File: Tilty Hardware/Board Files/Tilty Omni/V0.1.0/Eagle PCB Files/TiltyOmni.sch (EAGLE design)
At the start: 38 parts, among them U1 TEENSY_3.0_ALLPINSTEENSY_3.0_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, U2 HC-09_BREAKOUT, U4 LM2931, U5 MPU-6050, U7 SPI_FLASH-X25XXSMD

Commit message: Tilty omni work
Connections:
- net 5V_SCL: no longer JP7.11
- net 5V_SDA: now also JP7.11
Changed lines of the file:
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@@
 <label x="241.3" y="12.7" size="1.778" layer="95"/>
+</segment>
+<segment>
+<pinref part="JP7" gate="G$1" pin="11"/>
+<wire x1="302.26" y1="78.74" x2="312.42" y2="78.74" width="0.1524" layer="91"/>
+<label x="304.8" y="78.74" size="1.778" layer="95"/>
 </segment>
 </net>
@@
 </segment>
 <segment>
-<pinref part="JP7" gate="G$1" pin="11"/>
-<wire x1="302.26" y1="78.74" x2="312.42" y2="78.74" width="0.1524" layer="91"/>
-<label x="304.8" y="78.74" size="1.778" layer="95"/>
-</segment>
-<segment>

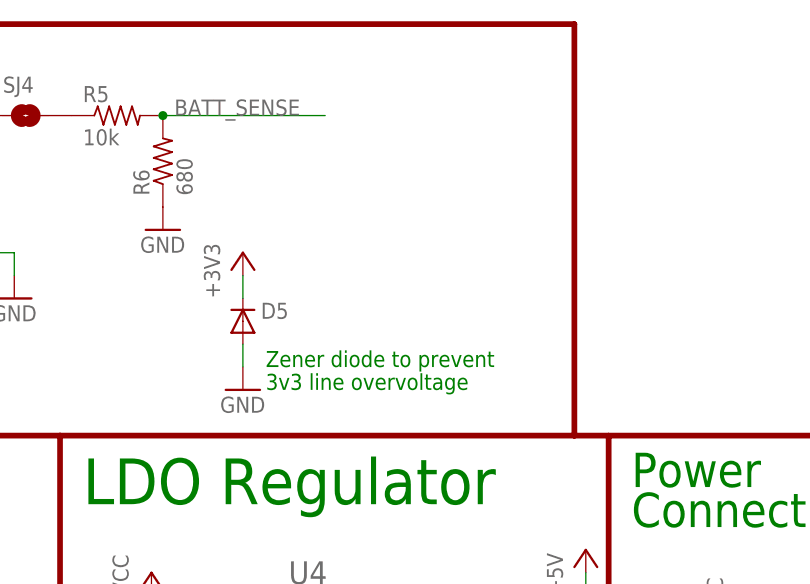
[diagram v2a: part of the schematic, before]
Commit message: Updated Tilty Duo/Quad Things.todo and moved a couple parts on Tilty Omni
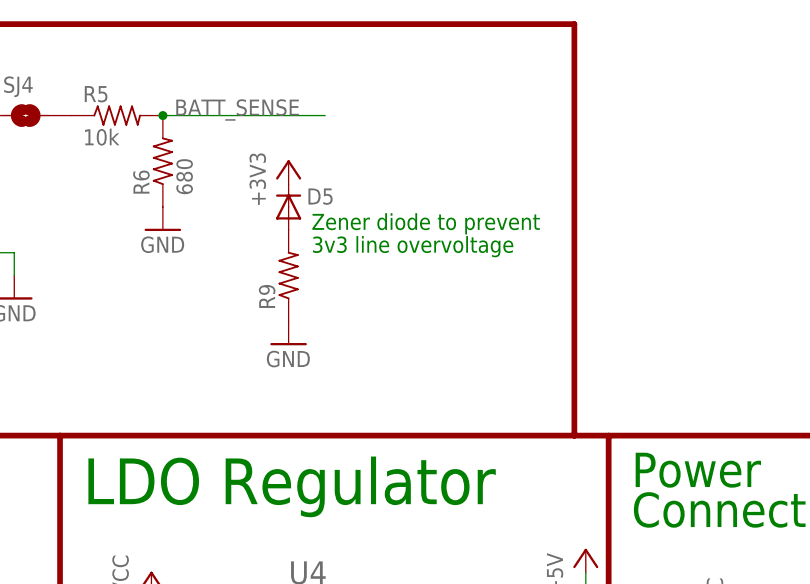
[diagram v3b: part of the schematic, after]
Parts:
- added R9: (no value), resistor:R-US_R0603
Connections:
- new net N$5: D5.A, R9.2
- net GND: now also R9.1; no longer D5.A
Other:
- moved on the sheet: D5
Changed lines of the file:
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@@
 <part name="P+9" library="supply1" deviceset="VCC" device=""/>
 <part name="GND5" library="supply1" deviceset="GND" device=""/>
+<part name="R9" library="resistor" deviceset="R-US_" device="R0603"/>
 </parts>
 <sheets>
@@
 <wire x1="212.725" y1="76.2" x2="172.72" y2="76.2" width="0.635" layer="94"/>
 <text x="7.62" y="172.72" size="5.08" layer="91" ratio="14">Flash Memory</text>
-<text x="134.62" y="142.24" size="1.778" layer="91">Zener diode to prevent</text>
-<text x="134.62" y="139.7" size="1.778" layer="91">3v3 line overvoltage</text>
+<text x="139.7" y="157.48" size="1.778" layer="91">Zener diode to prevent</text>
+<text x="139.7" y="154.94" size="1.778" layer="91">3v3 line overvoltage</text>
 <wire x1="1.27" y1="134.62" x2="1.27" y2="180.34" width="0.635" layer="94"/>
 <wire x1="69.85" y1="180.34" x2="1.27" y2="180.34" width="0.635" layer="94"/>
@@
 <instance part="SJ5" gate="A" x="91.44" y="139.7" rot="R270"/>
 <instance part="D4" gate="G$1" x="241.3" y="68.58" rot="R180"/>
-<instance part="D5" gate="G$1" x="132.08" y="147.32" smashed="yes" rot="R90">
-<attribute name="NAME" x="137.16" y="149.3774" size="1.778" layer="95" rot="R180"/>
-<attribute name="VALUE" x="134.3914" y="149.86" size="1.778" layer="96" rot="R90"/>
-<attribute name="PART#" x="132.08" y="147.32" size="1.778" layer="96" rot="R90" display="off"/>
-</instance>
-<instance part="GND23" gate="1" x="132.08" y="139.7"/>
+<instance part="D5" gate="G$1" x="137.16" y="160.02" smashed="yes" rot="R90">
+<attribute name="NAME" x="142.24" y="162.0774" size="1.778" layer="95" rot="R180"/>
+<attribute name="VALUE" x="139.4714" y="162.56" size="1.778" layer="96" rot="R90"/>
+<attribute name="PART#" x="137.16" y="160.02" size="1.778" layer="96" rot="R90" display="off"/>
+</instance>
+<instance part="GND23" gate="1" x="137.16" y="144.78"/>
 <instance part="U1" gate="G$1" x="208.28" y="38.1"/>
 <instance part="GND6" gate="1" x="152.4" y="15.24"/>
@@
 <instance part="+3V4" gate="G$1" x="53.34" y="167.64"/>
 <instance part="+3V5" gate="G$1" x="12.7" y="33.02"/>
-<instance part="+3V6" gate="G$1" x="132.08" y="154.94"/>
+<instance part="+3V6" gate="G$1" x="137.16" y="165.1"/>
 <instance part="P+4" gate="1" x="170.18" y="121.92"/>
 <instance part="P+5" gate="1" x="84.074" y="72.644" smashed="yes" rot="R270">
@@
 <instance part="P+9" gate="VCC" x="187.96" y="116.84"/>
 <instance part="GND5" gate="1" x="187.96" y="91.44"/>
+<instance part="R9" gate="G$1" x="137.16" y="152.4" rot="R90"/>
 </instances>
 <busses>
@@
 </segment>
 <segment>
-<pinref part="D5" gate="G$1" pin="A"/>
-<pinref part="GND23" gate="1" pin="GND"/>
-<wire x1="132.08" y1="142.24" x2="132.08" y2="144.78" width="0.1524" layer="91"/>
-</segment>
-<segment>
 <pinref part="JP2" gate="G$1" pin="8"/>
 <pinref part="GND8" gate="1" pin="GND"/>
@@
 <wire x1="279.4" y1="101.6" x2="269.24" y2="101.6" width="0.1524" layer="91"/>
 <label x="269.24" y="101.6" size="1.778" layer="95"/>
+</segment>
+<segment>
+<pinref part="R9" gate="G$1" pin="1"/>
+<pinref part="GND23" gate="1" pin="GND"/>
 </segment>
 </net>
@@
 <segment>
 <pinref part="D5" gate="G$1" pin="C"/>
-<wire x1="132.08" y1="149.86" x2="132.08" y2="152.4" width="0.1524" layer="91"/>
 <pinref part="+3V6" gate="G$1" pin="+3V3"/>
 </segment>
@@
 </segment>
 </net>
+<net name="N$5" class="0">
+<segment>
+<pinref part="D5" gate="G$1" pin="A"/>
+<pinref part="R9" gate="G$1" pin="2"/>
+</segment>
+</net>

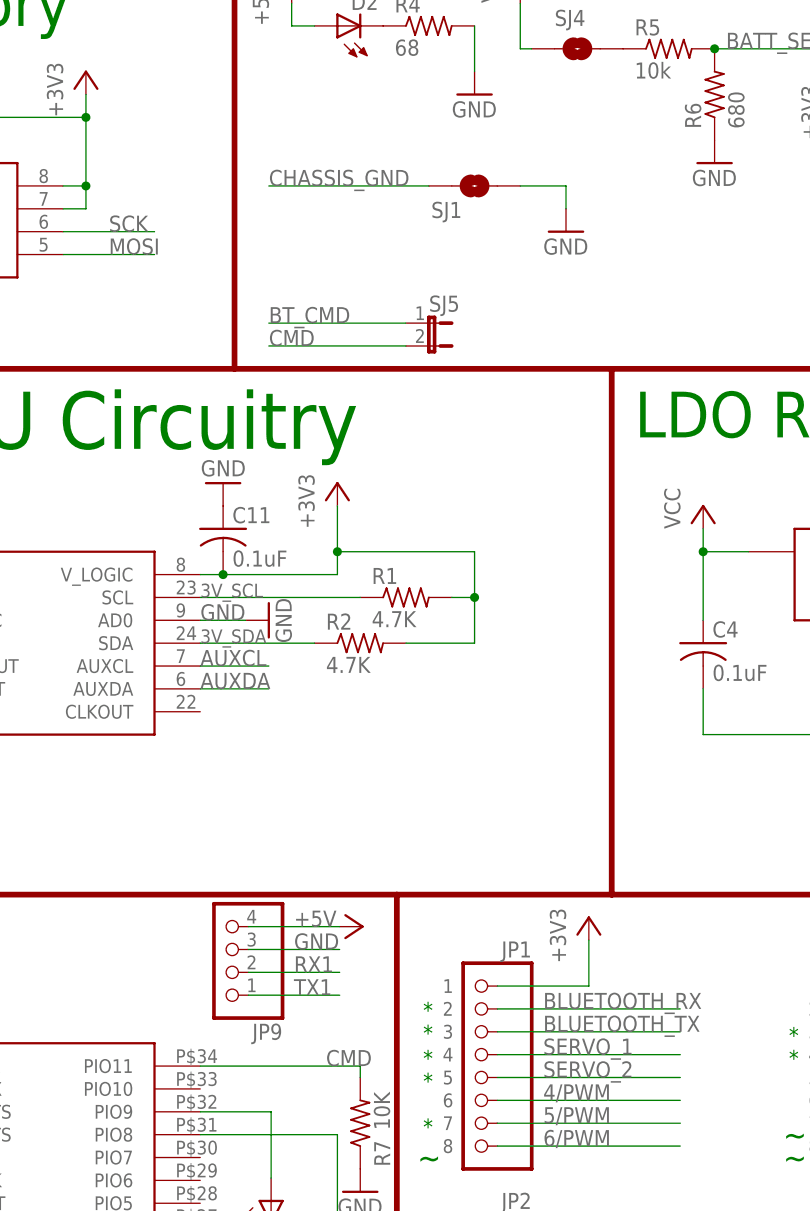
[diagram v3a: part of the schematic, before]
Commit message: Finished preliminary Tilty Omni design!
Still needs review before being ordered
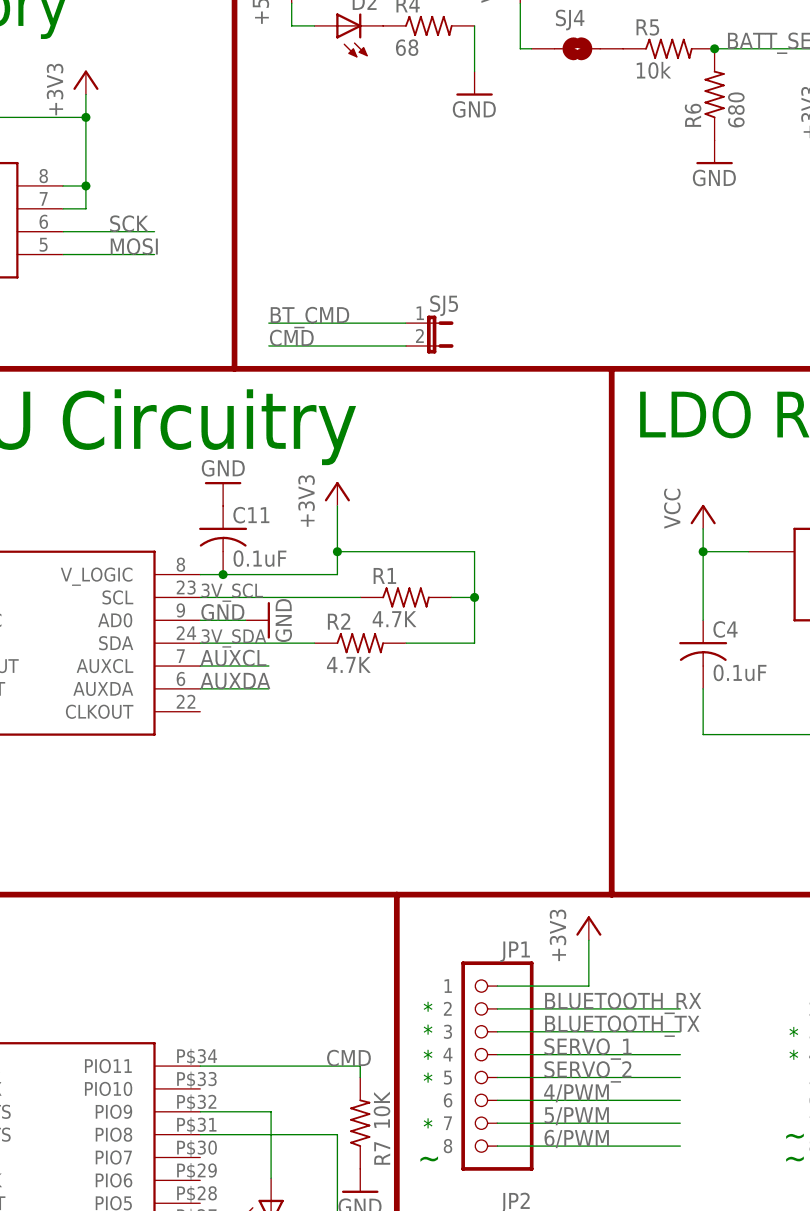
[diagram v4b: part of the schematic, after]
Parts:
- removed JP9: (no value), pinhead:PINHD-1X41X04_NO_SS_LOCKING
- removed SJ1: SOLDERJUMPERNO, SparkFun-Passives:SOLDERJUMPERNO
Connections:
- removed net CHASSIS_GND: SJ1.1
- removed net RX1: JP9.2
- removed net TX1: JP9.1
- net +5V: no longer JP9.4
- net GND: no longer JP9.3, SJ1.2
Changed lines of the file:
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@@
 <attribute name="RATED_VOLTAGE" value="2"/>
 </part>
-<part name="SJ1" library="SparkFun-Passives" deviceset="SOLDERJUMPER" device="NO"/>
-<part name="GND18" library="supply1" deviceset="GND" device=""/>
 <part name="GND19" library="supply1" deviceset="GND" device=""/>
 <part name="R7" library="resistor" deviceset="R-US_" device="R0603" value="10K"/>
@@
 <attribute name="RATED_VOLTAGE" value="2"/>
 </part>
-<part name="JP9" library="pinhead" deviceset="PINHD-1X4" device="1X04_NO_SS_LOCKING"/>
 <part name="R4" library="resistor" deviceset="R-US_" device="R0603" value="68"/>
 <part name="SJ4" library="SparkFun-Passives" deviceset="SOLDERJUMPER" device="TRACE"/>
@@
 <part name="+3V6" library="supply1" deviceset="+3V3" device=""/>
 <part name="P+4" library="supply1" deviceset="+5V" device=""/>
-<part name="P+5" library="supply1" deviceset="+5V" device=""/>
 <part name="JP6" library="SparkFun-Connectors" deviceset="M20" device=""/>
 <part name="JP7" library="SparkFun-Connectors" deviceset="M20" device=""/>
@@
 <attribute name="RATED_VOLTAGE" x="5.08" y="22.86" size="1.778" layer="96" display="off"/>
 </instance>
-<instance part="SJ1" gate="1" x="96.52" y="154.94" smashed="yes">
-<attribute name="NAME" x="91.694" y="151.384" size="1.778" layer="95"/>
-</instance>
-<instance part="GND18" gate="1" x="106.68" y="149.86"/>
 <instance part="GND19" gate="1" x="83.82" y="43.18"/>
 <instance part="R7" gate="G$1" x="83.82" y="50.8" smashed="yes" rot="R90">
@@
 <attribute name="RATED_VOLTAGE" x="12.7" y="162.56" size="1.778" layer="96" rot="R90" display="off"/>
 </instance>
-<instance part="JP9" gate="A" x="68.834" y="70.104" rot="R180"/>
 <instance part="R4" gate="G$1" x="91.44" y="172.72"/>
 <instance part="SJ4" gate="1" x="107.95" y="170.18" smashed="yes">
@@
 <instance part="+3V6" gate="G$1" x="137.16" y="165.1"/>
 <instance part="P+4" gate="1" x="170.18" y="121.92"/>
-<instance part="P+5" gate="1" x="84.074" y="72.644" smashed="yes" rot="R270">
-<attribute name="VALUE" x="76.454" y="72.644" size="1.778" layer="96"/>
-</instance>
 <instance part="JP6" gate="G$1" x="289.56" y="48.26" rot="MR0"/>
 <instance part="JP7" gate="G$1" x="292.1" y="48.26"/>
@@
 </segment>
 <segment>
-<pinref part="SJ1" gate="1" pin="2"/>
-<wire x1="101.6" y1="154.94" x2="106.68" y2="154.94" width="0.1524" layer="91"/>
-<wire x1="106.68" y1="154.94" x2="106.68" y2="152.4" width="0.1524" layer="91"/>
-<pinref part="GND18" gate="1" pin="GND"/>
-</segment>
-<segment>
-<wire x1="71.374" y1="70.104" x2="81.534" y2="70.104" width="0.1524" layer="91"/>
-<label x="76.454" y="70.104" size="1.778" layer="95"/>
-<pinref part="JP9" gate="A" pin="3"/>
-</segment>
-<segment>
 <pinref part="R7" gate="G$1" pin="1"/>
 <pinref part="GND19" gate="1" pin="GND"/>
@@
 <pinref part="MPU_INT" gate="1" pin="2"/>
 <wire x1="30.48" y1="109.22" x2="17.78" y2="109.22" width="0.1524" layer="91"/>
-</segment>
-</net>
-<net name="RX1" class="0">
-<segment>
-<wire x1="71.374" y1="67.564" x2="81.534" y2="67.564" width="0.1524" layer="91"/>
-<label x="76.454" y="67.564" size="1.778" layer="95"/>
-<pinref part="JP9" gate="A" pin="2"/>
-</segment>
-</net>
-<net name="TX1" class="0">
-<segment>
-<wire x1="71.374" y1="65.024" x2="81.534" y2="65.024" width="0.1524" layer="91"/>
-<label x="76.454" y="65.024" size="1.778" layer="95"/>
-<pinref part="JP9" gate="A" pin="1"/>
-</segment>
-</net>
-<net name="CHASSIS_GND" class="0">
-<segment>
-<pinref part="SJ1" gate="1" pin="1"/>
-<wire x1="91.44" y1="154.94" x2="73.66" y2="154.94" width="0.1524" layer="91"/>
-<label x="73.66" y="154.94" size="1.778" layer="95"/>
 </segment>
 </net>
@@
 </segment>
 <segment>
-<wire x1="71.374" y1="72.644" x2="81.534" y2="72.644" width="0.1524" layer="91"/>
-<pinref part="JP9" gate="A" pin="4"/>
-<pinref part="P+5" gate="1" pin="+5V"/>
-</segment>
-<segment>

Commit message: Made final revisions to Tilty Omni and R/C Receiver adapter before ordering!
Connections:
- net +5V: now also U1.VUSB
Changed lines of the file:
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@@
 <part name="GND5" library="supply1" deviceset="GND" device=""/>
 <part name="R9" library="resistor" deviceset="R-US_" device="R0603"/>
+<part name="P+5" library="supply1" deviceset="+5V" device=""/>
 </parts>
 <sheets>
@@
 <instance part="GND5" gate="1" x="187.96" y="91.44"/>
 <instance part="R9" gate="G$1" x="137.16" y="152.4" rot="R90"/>
+<instance part="P+5" gate="1" x="231.14" y="76.2"/>
 </instances>
 <busses>
@@
 <label x="307.34" y="101.6" size="1.778" layer="95"/>
 </segment>
-</net>
+<segment>
+<pinref part="P+5" gate="1" pin="+5V"/>
+<pinref part="U1" gate="G$1" pin="VUSB"/>
+<wire x1="231.14" y1="73.66" x2="231.14" y2="68.58" width="0.1524" layer="91"/>
+</segment>
+</net>
